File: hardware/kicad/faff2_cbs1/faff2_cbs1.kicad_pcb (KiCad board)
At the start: 4 copper layers, 210 x 130 mm, 412 parts, among them J1001 USB_C_Receptacle_USB2.0_16P, J1002 TSW-105-07-F-D, J1003 SAMTEC_SHF-107-01-L-D-SM, J1101 1x6 2.54mm, J1102 1x6 2.54mm, J1103 Micro-Fit 1x3, J201 KPJX-4S, J301 PH1-06-UA, J501 1729076, J502 8510-4500PL, J503 CONUFL001-SMD, J504 CONUFL001-SMD, J601 FH12-10S-0.5SH(55), J602 FTSH-105-01-L-DV-K-TR, J603 8510-4500PL, J701 1752120, J702 1752120, J703 8510-4500PL, J901 BTN EXT, J902 SMA Jack, J903 J-LIM, Q1101 BSZ099N06LS5, Q1102 BSZ099N06LS5, Q1103 BSZ099N06LS5, Q1104 BSZ099N06LS5, Q1105 BSZ099N06LS5, Q1106 BSZ099N06LS5, Q201 DMP6023LFG-7, SW1001 PTS526, SW901 PTS526, SW902 PTS526, SW903 PTS526, SW904 PTS526, U1001 STM32H723VET6, U1002 USB3320C, U1003 SRAM 32Mb, U1004 MIC5365-1.8, U1101 DRV8323S, U301 LMR33630, U302 ADPL42005, U303 ADPL42005, U304 LMR33630, U501 ADS1235, U601 AM26LV32, U701 ADS1120, U801 24FC16T-I/OT, U901 SN74LVC1G17, U902 SN74LVC1G11, Y1001 24MHz, Y1002 24MHz 18pF

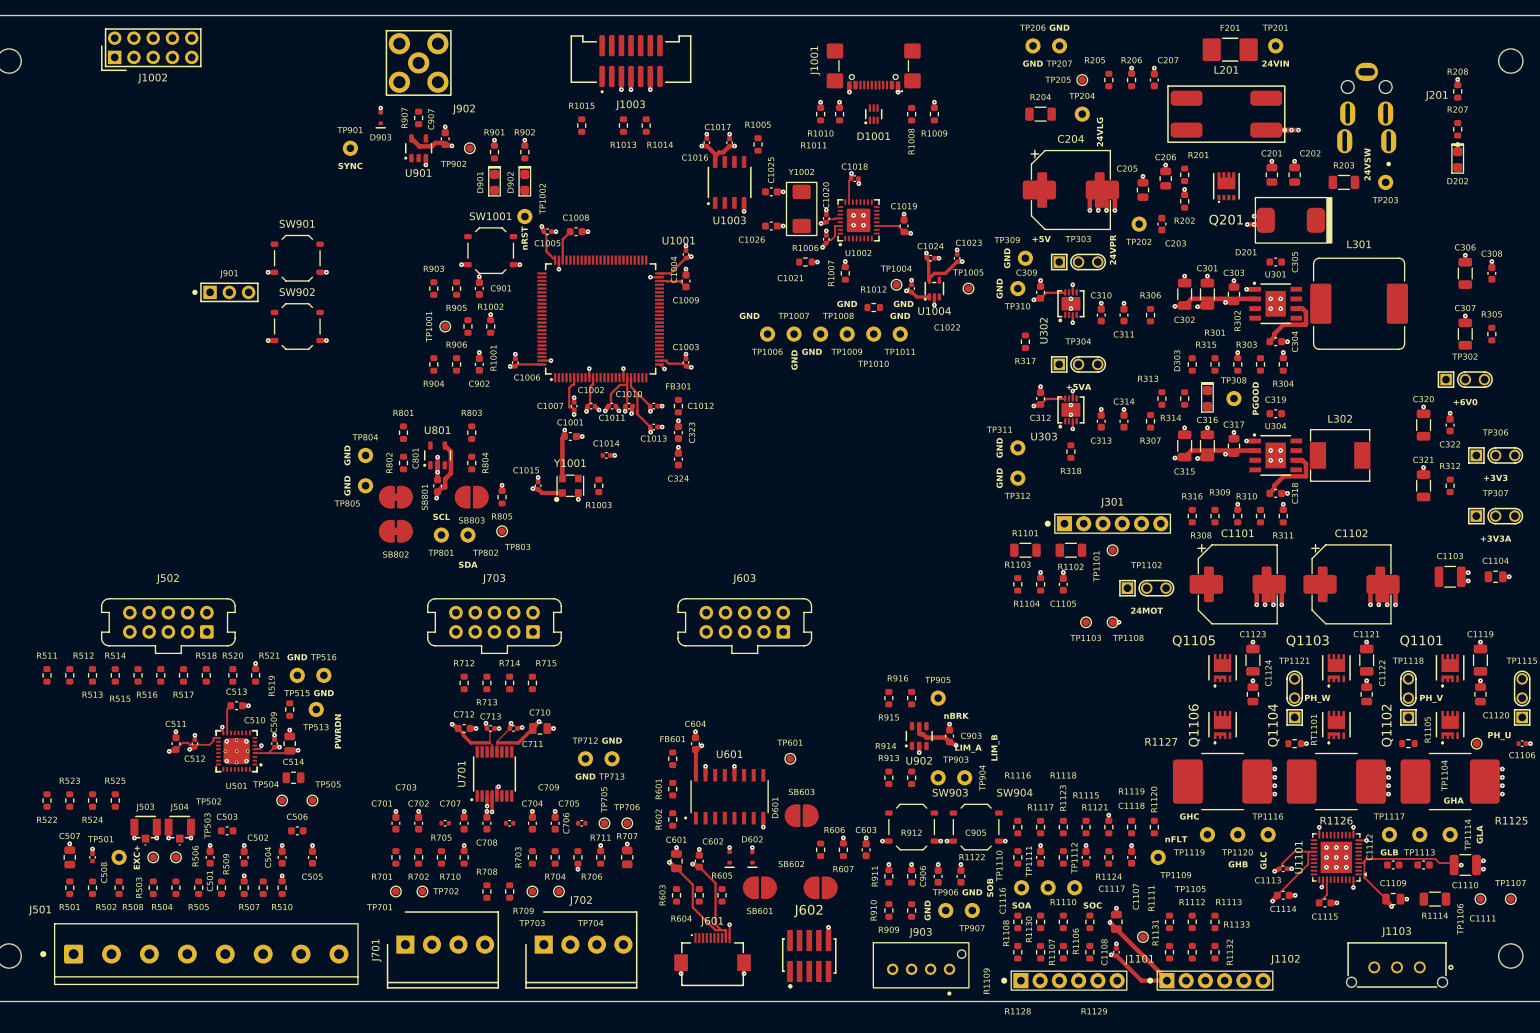
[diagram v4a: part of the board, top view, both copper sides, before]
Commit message: pcb: routing step 4 - the power distribution
Trunks first, in current-flow order and at IPC-2221 widths from the setup
file rather than from the net class alone: the 24 V entry chain, the motor
bus across the three high-side drains with its per-leg bypass in line, both
buck SW/output nodes and both LDO output chains.  Then the maze router
completes each rail onto the step-2 feed vias, with an F.Cu cost bias so the
long hauls settle on B.Cu under the traffic.

route_lib grows the pieces step 4 needed: a rasterised obstacle model over
real pad/track/via/hole copper, a two-layer A* with via and bend costs, a
pin-escape reservation pass and a fan-out pass so no trace can cap an IC's
pin ring, geometric per-net island analysis, and a repair pass on a re-read
board.  Steps 2 and 3 gain the same escape reservation.

Left open, and carried into the next stage: V24_MOT's last 8 mm to U1101.5,
the two LDO PGOOD pins, 24 vias that sit inside their own pad (via_mask
allows 0.25 mm to a pad where the proof demands 0.30), and three GND lands
that lost their via.  unconnected 388.

Co-Authored-By: Claude Opus 5 <noreply@anthropic.com>
Claude-Session: https://claude.ai/code/session_017QxCed5Tnu5nmeqhymaXHH
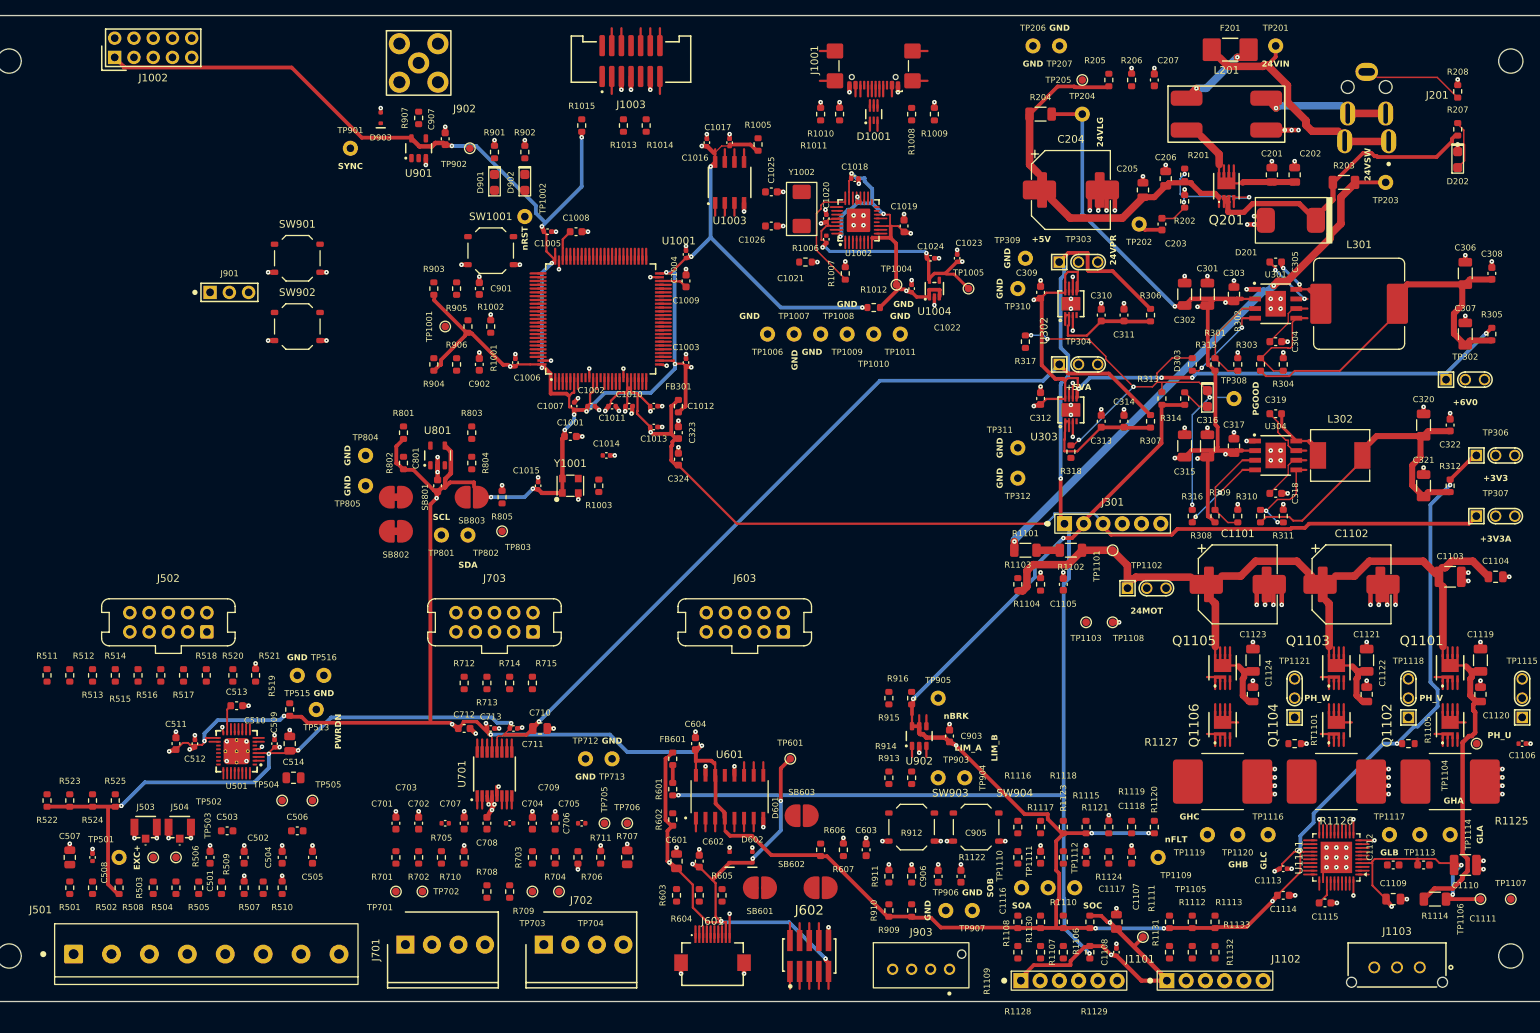
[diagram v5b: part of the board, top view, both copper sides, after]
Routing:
- net +3V3: track 103.0 -> 673.2 mm, vias 20 -> 39
- net +5VA: track 18.3 -> 194.3 mm, vias 4 -> 6
- net +5V: track 0.00 -> 163.2 mm, vias 0 -> 3
- net /motor_drive/V24_MOT: track 0.00 -> 158.5 mm
- net +3V3A: track 20.4 -> 144.1 mm, vias 4 -> 5
- net /power_entry_24v/V24_PROT: track 0.00 -> 89.3 mm
- net /power_rails/+6V0: track 8.71 -> 95.8 mm, vias 2 -> 6
- net /power_entry_24v/+24V_SW: track 0.00 -> 71.9 mm, vias 0 -> 2
- net /power_rails/RAIL_PGOOD: track 0.00 -> 65.9 mm, vias 0 -> 6
- net /power_entry_24v/V24_LOGIC: track 28.8 -> 91.0 mm
- net /linear_encoder/+5V_ENC: track 24.1 -> 79.0 mm, vias 2 -> 6
- net Net-(C306-Pad1): track 0.00 -> 43.5 mm
- net /mcu/+3V3_USB: track 11.7 -> 54.4 mm, vias 3 -> 6
- net Net-(C320-Pad1): track 0.00 -> 39.1 mm
- net /power_entry_24v/V24_IN: track 0.00 -> 28.1 mm
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
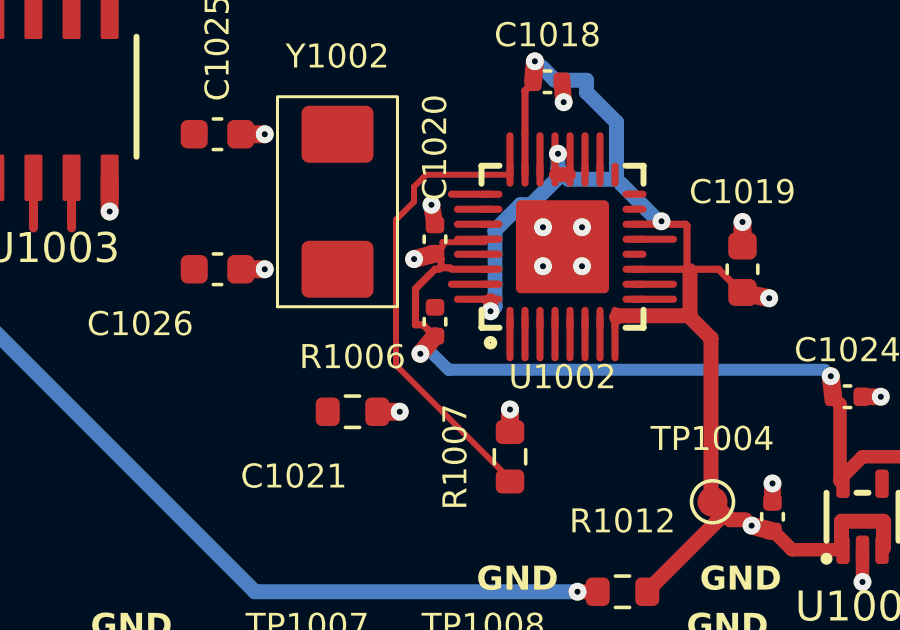
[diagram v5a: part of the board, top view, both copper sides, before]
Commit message: pcb: routing step 3b - close the ground-via completeness proof
Step 3 left C1021 pad 2 with no answer: the PHY's +1V8 decoupler is walled in
by that rail's own feed on the north and by the USB3320 bias run on the west,
and step 3's search only ever looks in-line, then swung about the in-line
axis.  Widening it to "any legal via slot within reach, with a maze-routed
stub" finds one 0.87 mm east-south-east, which no swing was going to reach --
`tools/route3b_gndfix.py`, run over whatever lands the proof still reports.

Two proofs corrected to measure the physical thing rather than a proxy:

  * via-in-pad was flagging any via whose *copper* touched a pad, so 24
    same-net G1d hugs read as defects.  What wicks solder is a barrel that
    opens into a land, and what breaks clearance is copper on a foreign pad;
    both are now separate hard failures, and the same-net hug is counted and
    listed instead (closest 0.275 mm, barrel 0.475 mm clear of the land).
  * GND completeness now follows the R-C3-1 exposed-pad tie through to the
    EP's via array rather than reporting U1101 pad 32 as uncovered, and
    asserts that a group of lands sharing one stub island still owns one via
    per land -- C801/U801 and C708/U701 are the G4b decoupling loop, not the
    shared via R4-1 forbids.

Left: D1001 pad 2, whose via is part of step 5's USB pair geometry.

Co-Authored-By: Claude Opus 5 <noreply@anthropic.com>
Claude-Session: https://claude.ai/code/session_017QxCed5Tnu5nmeqhymaXHH
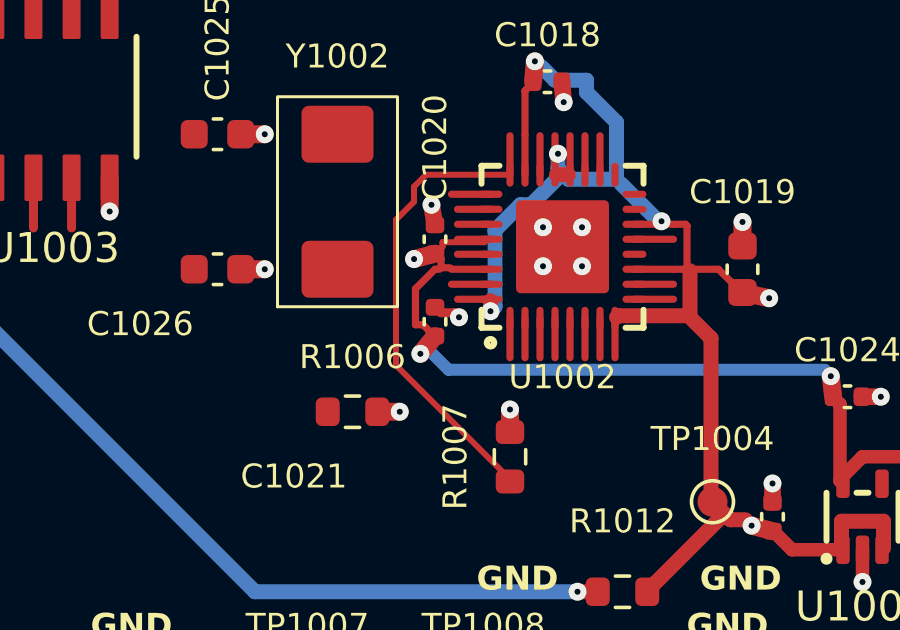
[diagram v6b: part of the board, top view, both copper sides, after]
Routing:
- net GND: track 260.1 -> 260.9 mm, vias 252 -> 253
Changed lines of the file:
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@@
+	)
+	(segment
+		(start 144.4 59.2)
+		(end 144.45 59.25)
+		(width 0.3)
+		(layer "F.Cu")
+		(net 118)
 	)
 	(segment
@@
 	)
 	(segment
+		(start 143.95 59.2)
+		(end 144.4 59.2)
+		(width 0.3)
+		(layer "F.Cu")
+		(net 118)
+	)
+	(segment
 		(start 200.575 130.449999)
 		(end 202.895 130.449999)
@@
 	)
 	(segment
+		(start 143.8 59.05)
+		(end 143.95 59.2)
+		(width 0.3)
+		(layer "F.Cu")
+		(net 118)
+	)
+	(segment
 		(start 181.5 110)
 		(end 182.35 110)
@@
 		(size 0.6)
 		(drill 0.2)
+		(layers "F.Cu" "B.Cu")
+		(net 118)
+	)
+	(via
+		(at 144.55 59.35)
+		(size 0.6)
+		(drill 0.2)
